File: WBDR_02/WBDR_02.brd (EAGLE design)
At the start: 30.9 x 64 mm, 39 parts, among them IC2 DIO6970TST6, IC3 SN65HVD232D, IC4 DS3231M+TRL, IC5 AT24C32D-SSHM-B, IC7 DS05-127-2-04BK-SMT-TR

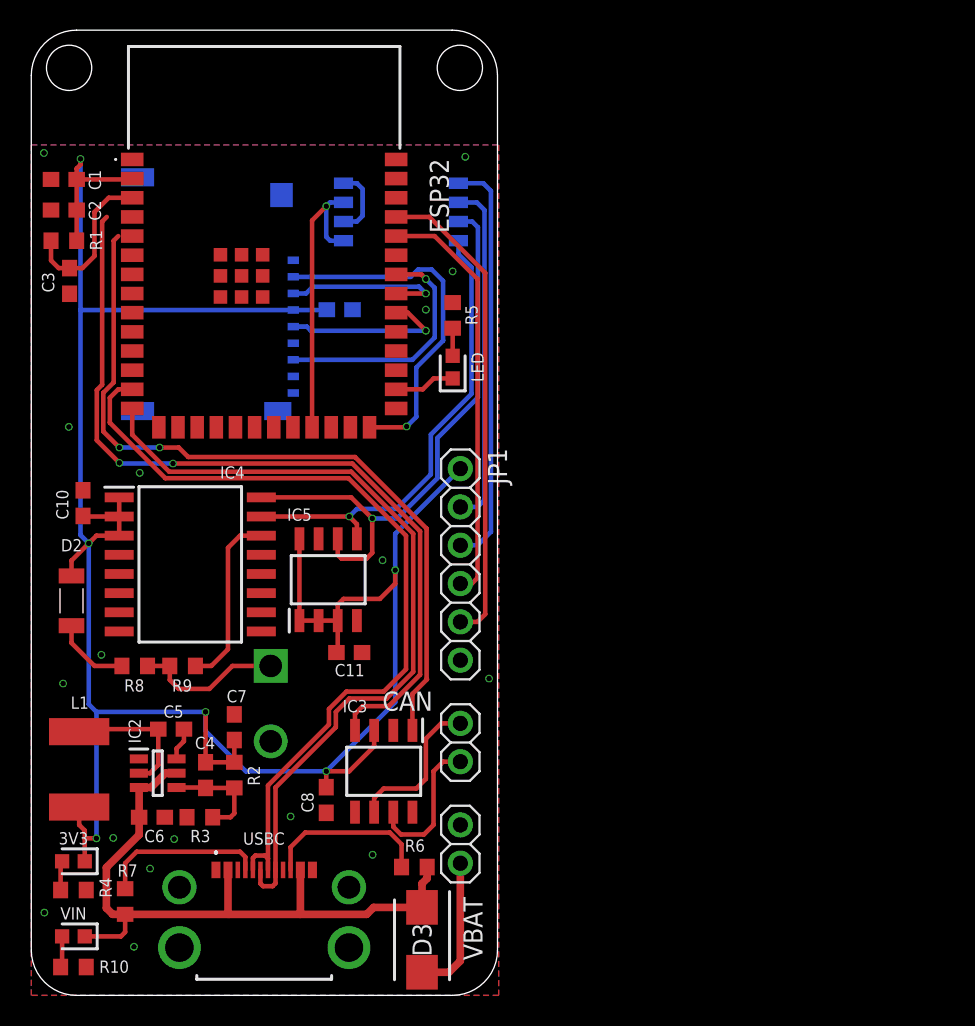
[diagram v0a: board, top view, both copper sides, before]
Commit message: Change CAN and add new board WBDR
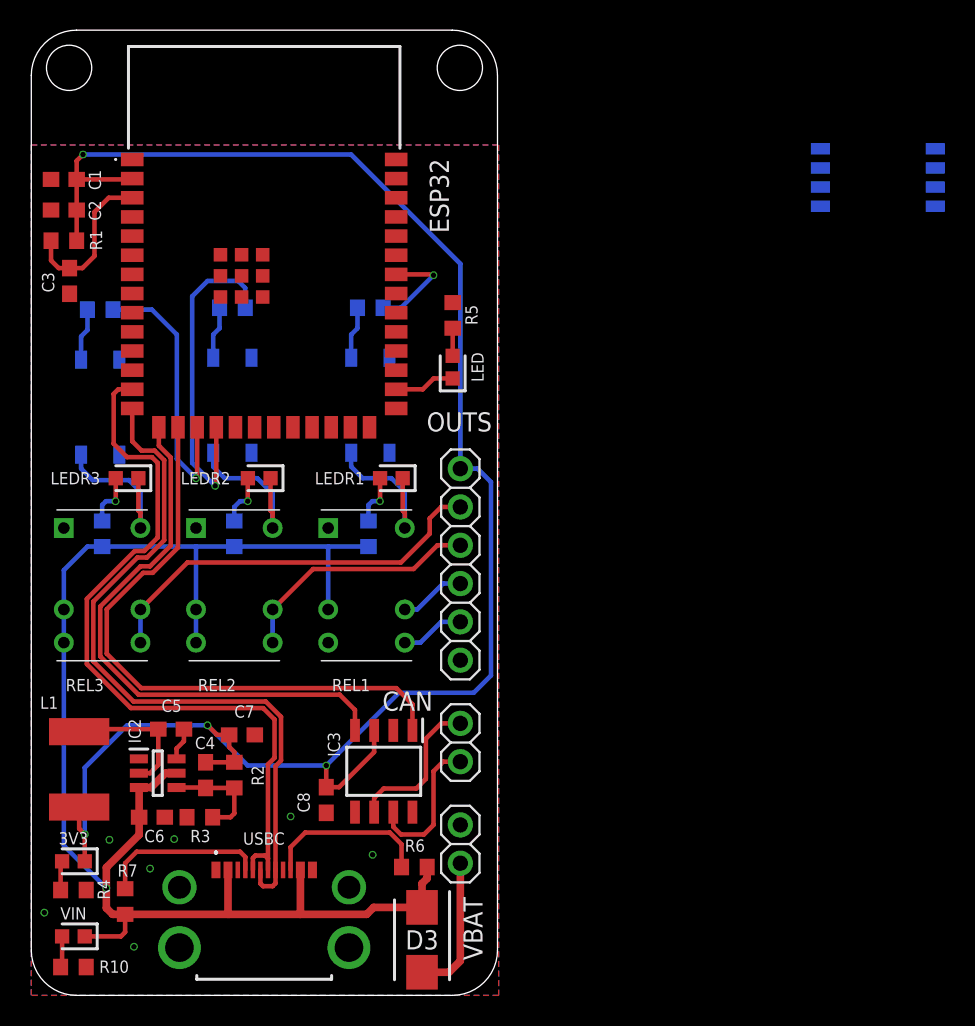
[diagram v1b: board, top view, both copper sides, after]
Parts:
- removed C10, C11, C9: 0.1uF, rcl:C0603
- removed D2: BAS85,115, SamacSys_Parts:BAS85115
- removed MICROSD: MICROSD-PUSH-OUT, microsd:MICROSD-PUSH-OUT
- removed R8: 2k2, rcl:R0603
- removed R9: 1k, rcl:R0603
- removed SUPERCAPACITOR: 5V5 1F, SamacSys_Parts:CAPPRD500W130D2150H800
- added IC1: TLP175A_TPL,E, SamacSys_Parts:TLP266J
- added LEDR1, LEDR2, LEDR3: 150060GS75000, SamacSys_Parts:LEDC1608X80N
- added R14, R16, R18: 2k4, rcl:R0603
- added R15, R17, R19: 330, rcl:R0603
- added REL1, REL2, REL3: 1462043-8, SamacSys_Parts:14620438
- IC4: value DS3231M+TRL -> TLP175A_TPL,E; device SamacSys_Parts:SOIC127P1032X265-16N -> SamacSys_Parts:TLP266J
- IC5: value AT24C32D-SSHM-B -> TLP175A_TPL,E; device SamacSys_Parts:SOIC127P600X175-8N -> SamacSys_Parts:TLP266J
- moved IC7 31.7 mm to (56.1, 54.2)
- moved IC5 19.3 mm to (4.57, 39.6), flipped to the bottom, turned to 270 degrees
- moved IC4 11.5 mm to (13.3, 39.8), flipped to the bottom, turned to 270 degrees
- moved C7 0.72 mm to (14.0, 17.3), turned to 0 degrees
- renumbered JP1 to OUTS
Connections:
- removed net MTCK: ESP32.32, MICROSD.5
- removed net MTDI: ESP32.34, MICROSD.7
- removed net MTDO: ESP32.33, MICROSD.3
- removed net RTCBAT: R8.1, R9.2, SUPERCAPACITOR.1
- removed net RTCD: D2.2, R8.2
- removed net SDCARD: ESP32.26, MICROSD.2
- removed net VBAT: IC4.14, R9.1
- new net COIL1: IC1.6, LEDR1.1, REL1.8
- new net COIL2: IC4.6, LEDR2.1, REL2.8
- new net COIL3: IC5.6, LEDR3.1, REL3.8
- new net LEDCOIL1: LEDR1.2, R14.1
- new net LEDCOIL2: LEDR2.2, R16.1
- new net LEDCOIL3: LEDR3.2, R18.1
- new net O1: OUTS.5, REL1.5
- new net O2: OUTS.4, REL1.6
- new net O3: OUTS.3, REL2.5, REL2.6
- new net O4: OUTS.2, REL3.5, REL3.6
- new net OUT1: ESP32.34, R15.1
- new net OUT2: ESP32.18, R17.1
- new net OUT3: ESP32.17, R19.1
- new net OUTO1: IC1.1, R15.2
- new net OUTO2: IC4.1, R17.2
- new net OUTO3: IC5.1, R19.2
- net +3V3: no longer C10.1, C11.1, C9.1, D2.1, IC4.1, IC4.2, IC4.3, IC5.1, IC5.2, IC5.3, IC5.8, MICROSD.4
- net CANRX: now also ESP32.15; no longer ESP32.8
- net CANTX: now also ESP32.16; no longer ESP32.9
- net GND: now also IC1.3, IC1.4, IC4.3, IC4.4, IC5.3, REL1.1, REL1.4, REL2.1, REL3.1; no longer C10.2, C11.2, C9.2, IC4.10, IC4.11, IC4.12, IC4.13, IC4.5, IC4.6, IC4.7, IC4.8, IC4.9, IC5.7, MICROSD.6, MICROSD.G1, MICROSD.G2, MICROSD.G3, MICROSD.G4, SUPERCAPACITOR.2
- net RX: no longer OUTS.4
- net SCL1: no longer IC4.16, IC5.6
- net SCL2: no longer OUTS.3
- net SDA: no longer ESP32.23
- net SDA1: no longer IC4.15, IC5.5
- net SDA2: no longer OUTS.2
- net TX: no longer OUTS.5
- net VIN: now also R14.2, R16.2, R18.2, REL1.3, REL2.3, REL2.4, REL3.3, REL3.4
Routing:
- net VIN: track 45.8 -> 99.4 mm, vias 0 -> 1
- net SCL1: track 38.5 -> 0.00 mm, vias 1 -> 0
- net +3V3: track 156.2 -> 118.8 mm, vias 6 -> 4
- net TX: track 31.9 -> 0.00 mm
- net SDA1: track 31.1 -> 0.00 mm, vias 1 -> 0
- net RX: track 27.7 -> 0.00 mm
- net SCL2: track 27.4 -> 0.00 mm
- net O4: track 0.00 -> 26.8 mm
- net SDCARD: track 23.6 -> 0.00 mm, vias 1 -> 0
- net SDA2: track 23.0 -> 0.00 mm
- net OUT2: track 0.00 -> 22.7 mm, vias 0 -> 1
- net SDA: track 19.6 -> 0.00 mm, vias 1 -> 0
- net OUT3: track 0.00 -> 18.4 mm, vias 0 -> 1
- net CANRX: track 55.0 -> 37.5 mm, vias 2 -> 0
- net O3: track 0.00 -> 16.4 mm
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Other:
- board text added: "WBDR v02"
- board text removed: "WBD v02"

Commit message: HW finished
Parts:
- removed IC7: DS05-127-2-04BK-SMT-TR, SamacSys_Parts:DS05127204BKSMTTR
- renumbered REL1 to RELAY1, REL2 to RELAY2, REL3 to RELAY3
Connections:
- removed net O4: OUTS.2, RELAY3.5, RELAY3.6
- removed net SCL: IC7.3, IC7.7
- removed net SCL1: IC7.4
- removed net SCL2: IC7.8
- removed net SDA: IC7.1, IC7.5
- removed net SDA1: IC7.2
- removed net SDA2: IC7.6
- new net IN1: OUTS.5, RELAY1.5, RELAY1.6
- new net IN2: OUTS.3, RELAY2.5, RELAY2.6
- net +3V3: no longer OUTS.1
- net GND: no longer RELAY1.4
- net O1: now also OUTS.4, RELAY1.3, RELAY1.4; no longer OUTS.5, RELAY1.5
- net O2: now also OUTS.2, RELAY2.3, RELAY2.4; no longer OUTS.4, RELAY1.6
- net O3: now also OUTS.1, RELAY3.5, RELAY3.6; no longer OUTS.3, RELAY2.5, RELAY2.6
- net VIN: no longer RELAY1.3, RELAY2.3, RELAY2.4
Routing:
- net O4: track 26.8 -> 0.00 mm
- net +3V3: track 118.8 -> 94.4 mm, vias 4 -> 5
- net O2: track 4.39 -> 23.4 mm
- net IN2: track 0.00 -> 16.4 mm
- net O3: track 16.4 -> 29.8 mm
- net VIN: track 99.4 -> 89.1 mm
- net O1: track 4.25 -> 11.7 mm
- net IN1: track 0.00 -> 6.22 mm
- net OUT3: track 18.4 -> 21.4 mm
- net OUT2: track 22.7 -> 24.6 mm
